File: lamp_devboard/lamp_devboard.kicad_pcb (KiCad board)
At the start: 2 copper layers, 127 parts, among them J101 Conn_02x02_Counter_Clockwise, J102 Conn_02x02_Counter_Clockwise, J103 Conn_02x02_Counter_Clockwise, J104 Conn_02x02_Counter_Clockwise, J105 Conn_02x02_Counter_Clockwise, J106 Conn_02x02_Counter_Clockwise, J201 Screw_Terminal_01x02, J202 USB_C_Receptacle_USB2.0, J203 Conn_01x03, J901 Conn_02x05_Odd_Even, J902 Conn_01x03, J903 Conn_01x06, J904 Conn_01x06, J905 Conn_01x06, J906 Conn_01x05, SW1001 SW_Push, SW1002 SW_Push, SW1003 SW_Push, U201 TPS212x, U202 BQ24200, U203 FUSB302B01MPX, U204 TLV71318PDBV, U205 TLV71318PDBV, U301 MAX9938, U401 TPS63060, U501 MAX9938, U601 TPS63060, U701 MAX9938, U901 STM32L476RG, Y901 Crystal_GND2, Y902 Crystal_GND2

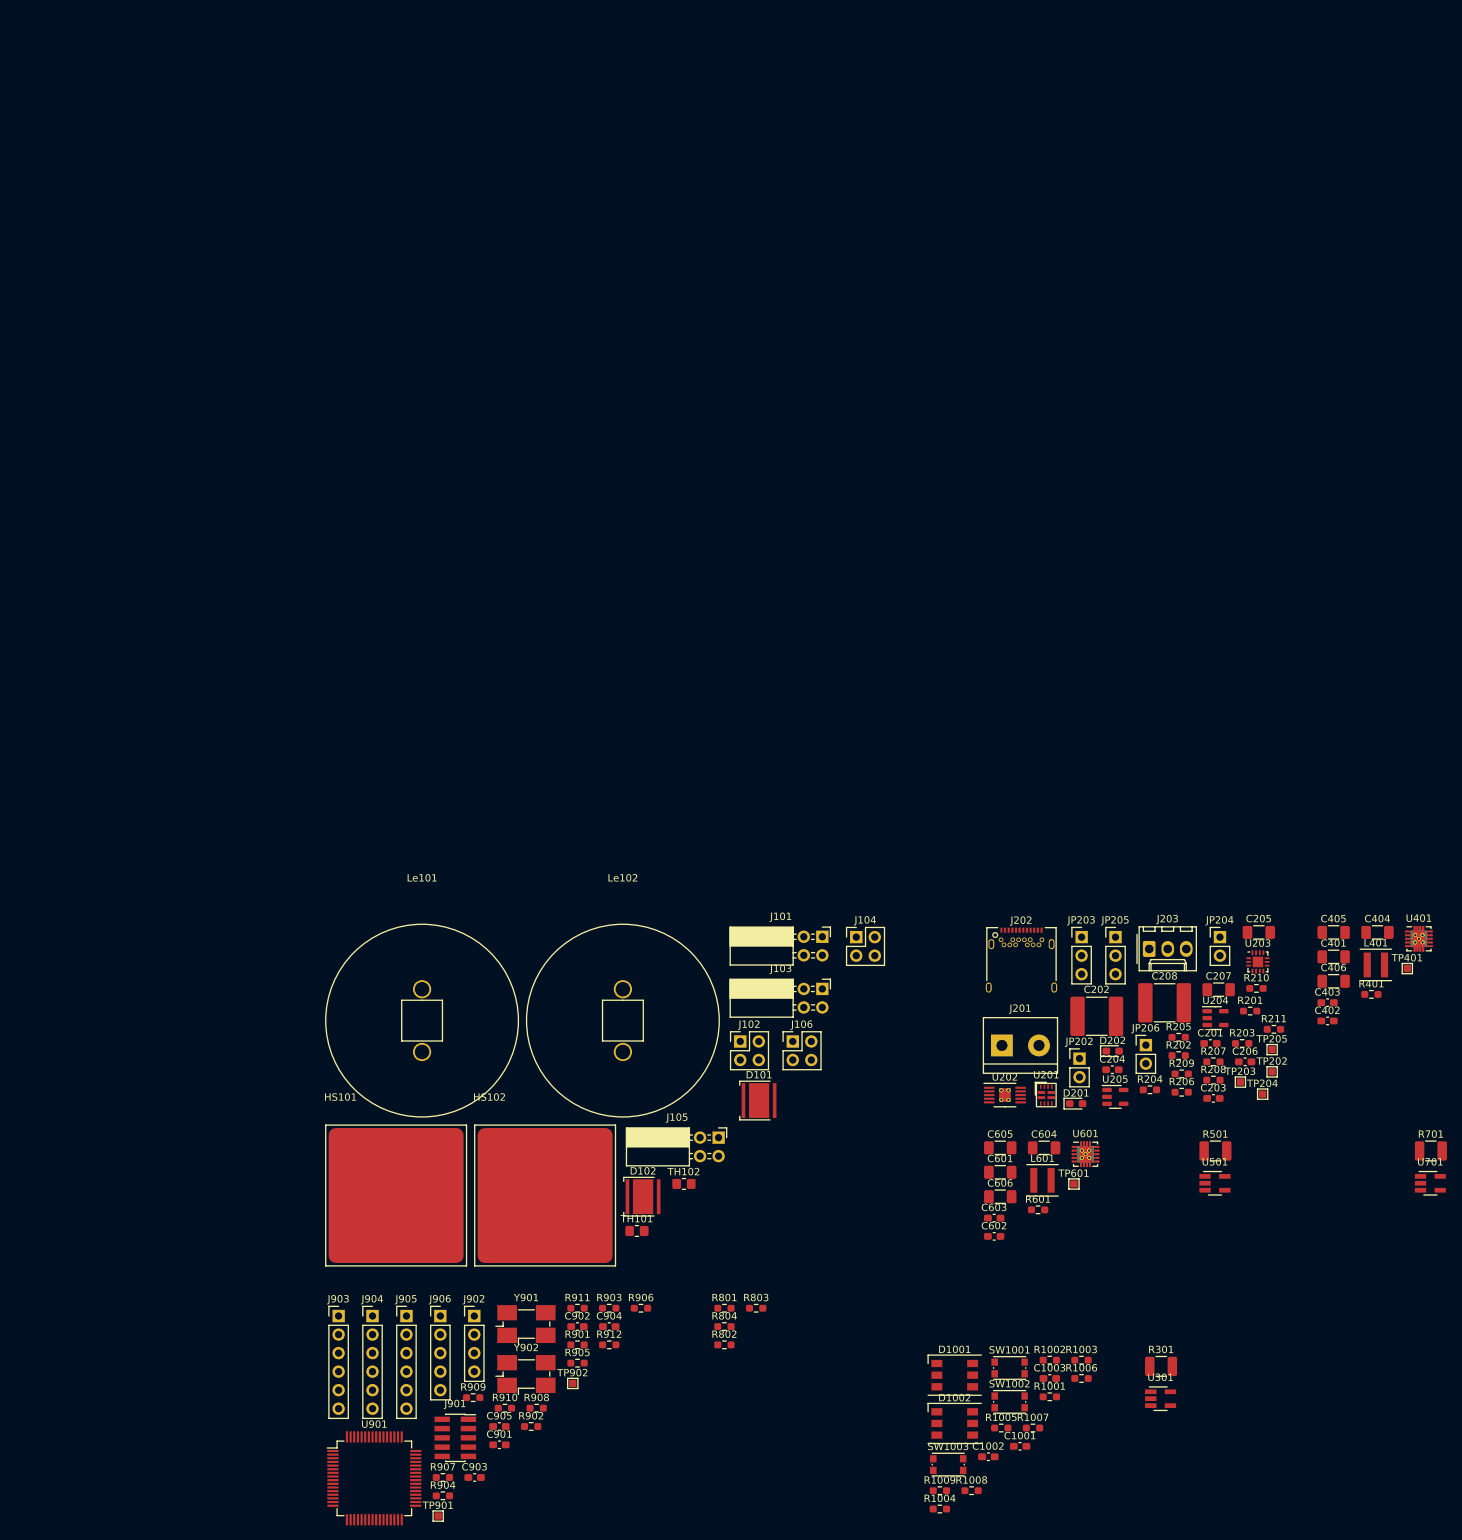
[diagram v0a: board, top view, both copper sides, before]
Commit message: place components
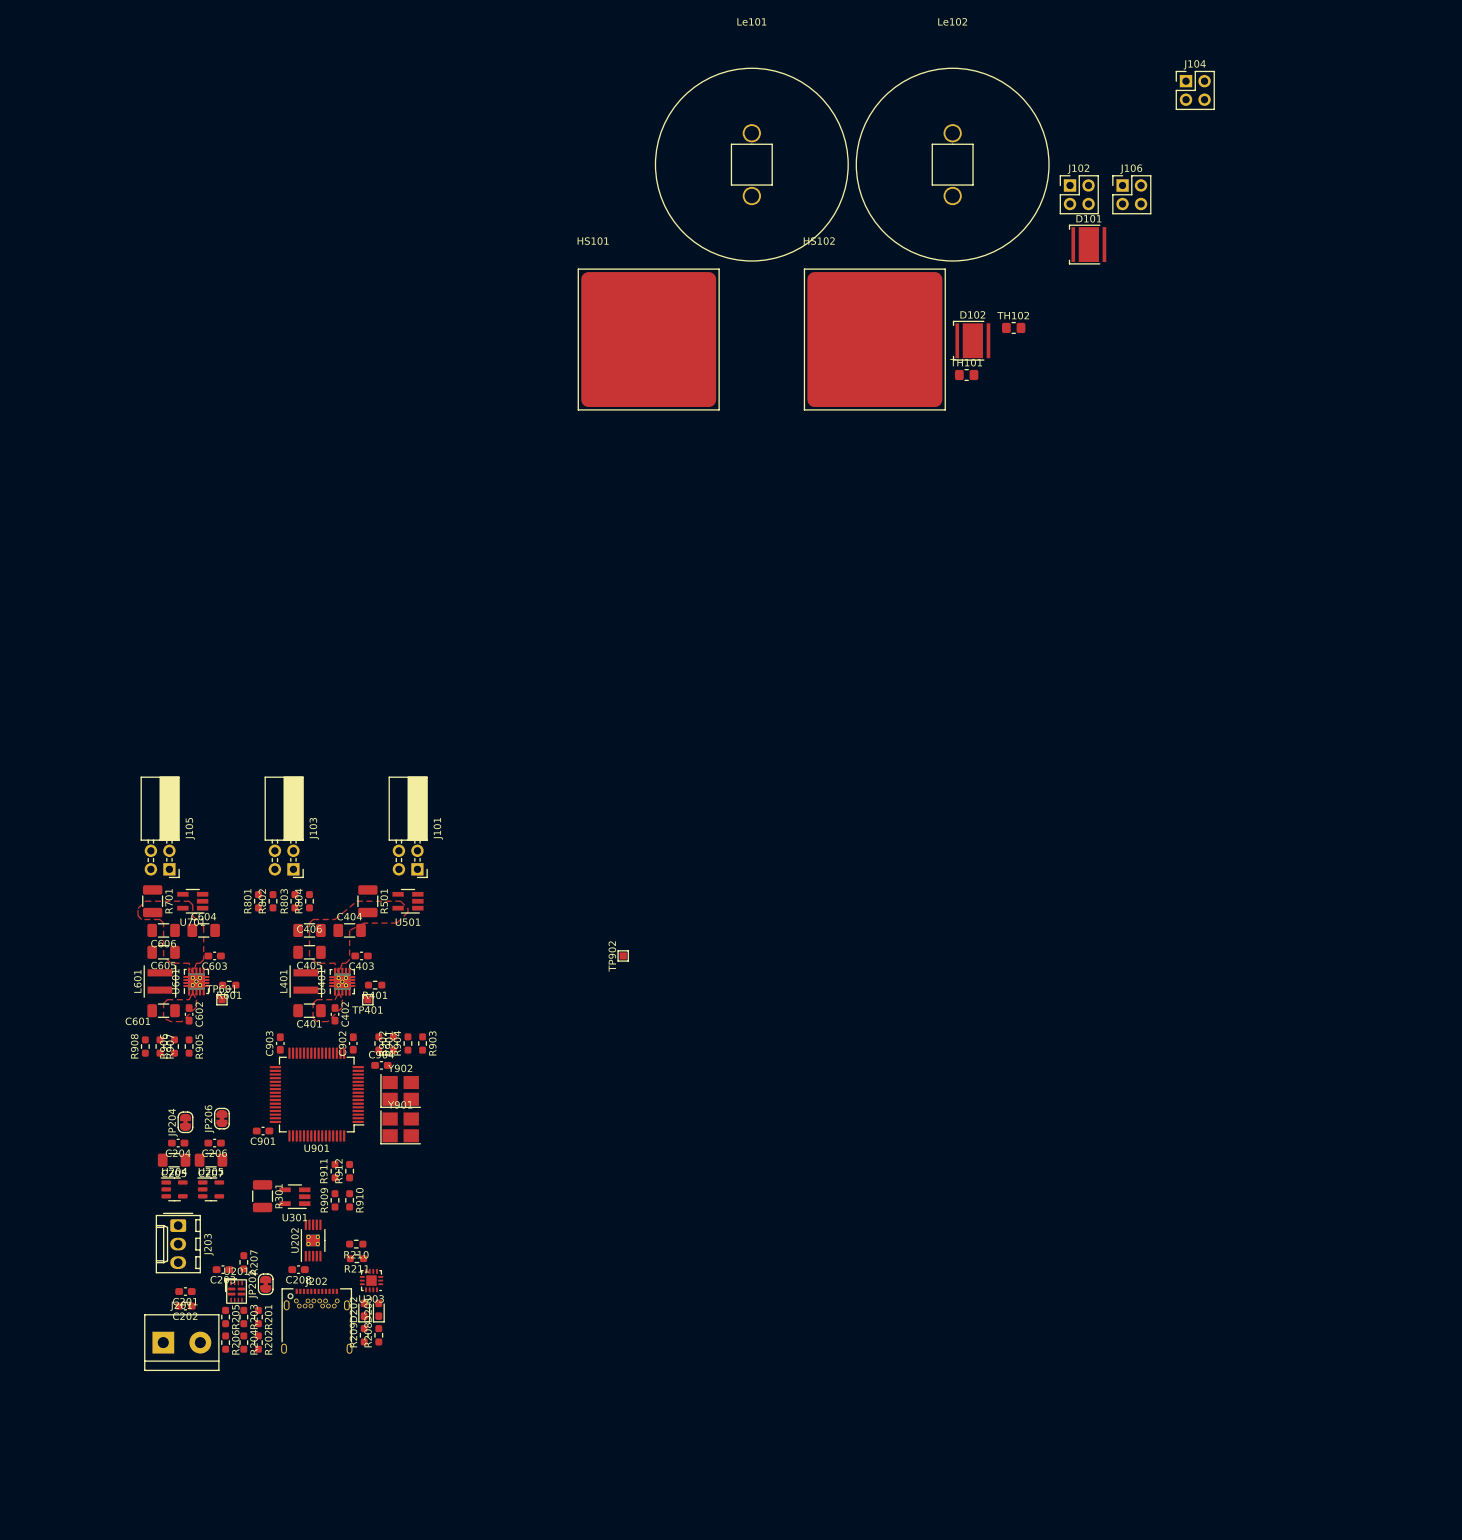
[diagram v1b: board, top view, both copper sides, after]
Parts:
- removed C1001, C1002, C1003, C905: C, Capacitor_SMD:C_0603_1608Metric_Pad1.08x0.95mm_HandSolder
- removed D1001, D1002: LED_RGB, LED_SMD:LED_WS2812_PLCC6_5.0x5.0mm_P1.6mm
- removed J901: Conn_02x05_Odd_Even, Connector_PinSocket_1.27mm:PinSocket_2x05_P1.27mm_Vertical_SMD
- removed J902: Conn_01x03, Connector_PinHeader_2.54mm:PinHeader_1x04_P2.54mm_Vertical
- removed J903, J904, J905: Conn_01x06, Connector_PinHeader_2.54mm:PinHeader_1x06_P2.54mm_Vertical
- removed J906: Conn_01x05, Connector_PinHeader_2.54mm:PinHeader_1x05_P2.54mm_Vertical
- removed JP203, JP205: Jumper_3_Open, Connector_PinHeader_2.54mm:PinHeader_1x03_P2.54mm_Vertical
- removed R1001, R1002, R1003, R1004, R1005, R1006, R1007, R1008, R1009: R, Resistor_SMD:R_0603_1608Metric_Pad0.98x0.95mm_HandSolder
- removed SW1001, SW1002, SW1003: SW_Push, Button_Switch_SMD:SW_Push_1P1T_NO_CK_KMR2
- removed TP202, TP203, TP204, TP205, TP901: TestPoint, TestPoint:TestPoint_Pad_1.0x1.0mm
- C202, C208: footprint Capacitor_SMD:C_2220_5650Metric_Pad1.97x5.40mm_HandSolder -> Capacitor_SMD:C_0603_1608Metric_Pad1.08x0.95mm_HandSolder
- JP202, JP204, JP206: footprint Connector_PinHeader_2.54mm:PinHeader_1x02_P2.54mm_Vertical -> Jumper:SolderJumper-2_P1.3mm_Bridged_RoundedPad1.0x1.5mm
- Y901, Y902: footprint Crystal:Crystal_SMD_0603-4Pin_6.0x3.5mm_HandSoldering -> Crystal:Crystal_SMD_3225-4Pin_3.2x2.5mm_HandSoldering
- moved R701 178.5 mm to (42.0, 42.5), turned to -90 degrees
- moved U701 174.0 mm to (47.5, 42.5), turned to 180 degrees
- moved C205 151.9 mm to (44.9, 78.0), turned to 180 degrees
- moved U401 147.7 mm to (68.0, 53.5), turned to 90 degrees
- moved L401 146.7 mm to (63.0, 53.5), turned to 90 degrees
- moved U204 144.6 mm to (45.0, 82.0)
- moved C201 144.6 mm to (46.5, 96.0), turned to 180 degrees
- moved JP204 144.1 mm to (46.5, 72.8), turned to 90 degrees
- moved TP401 142.6 mm to (71.5, 56.0), turned to 180 degrees
- moved R201 142.3 mm to (56.5, 99.5), turned to -90 degrees
- moved R203 141.9 mm to (54.5, 99.5), turned to -90 degrees
- moved C206 141.7 mm to (50.5, 75.7), turned to 180 degrees
- moved C404 140.9 mm to (69.0, 46.5)
- moved C401 140.6 mm to (63.5, 57.5), turned to 180 degrees
- moved C406 140.6 mm to (63.5, 46.5), turned to 180 degrees
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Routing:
- added copper zone on F.Cu, net /current_probe_1/IV_Iin
- added copper zone on F.Cu, net /current_probe_2/IV_Iin
- added copper zone on F.Cu, net /current_probe_in/IV_Iout

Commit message: add some power polygones to the pcb
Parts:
- moved J203 20.1 mm to (60.9, 99.9)
- moved JP202 7.82 mm to (57.0, 87.2)
- moved U202 6.05 mm to (61.7, 94.6), turned to -90 degrees
- moved R210 5.60 mm to (75.5, 89.5)
- moved D201 5.60 mm to (78.6, 98.5)
- moved D202 5.60 mm to (76.6, 98.5)
- moved R208 5.60 mm to (78.6, 102.0)
- moved R209 5.60 mm to (76.6, 102.0)
- moved R211 5.60 mm to (75.6, 91.5)
- moved U203 5.60 mm to (77.6, 94.5)
- moved J202 5.40 mm to (69.9, 101.0)
- moved C208 5.00 mm to (67.0, 93.0)
- moved JP206 2.12 mm to (49.4, 72.6)
- moved JP204 2.10 mm to (44.4, 72.8)
- moved C204 2.00 mm to (43.5, 75.7)
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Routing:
- net /current_probe_in/IV_Iin: track 0.00 -> 7.61 mm
- net Net-(C201-Pad1): track 0.00 -> 5.71 mm
- net /current_probe_in/IV_Out: track 0.00 -> 4.83 mm
- net Net-(J203-Pad1): track 0.00 -> 2.68 mm
- net /uC/Vout2: track 0.00 -> 2.00 mm
- net /uC/Vout1: track 0.00 -> 2.00 mm
- net /uC/Vin: track 0.00 -> 2.00 mm
- net /uC/Iout2: track 0.00 -> 2.00 mm
- net /uC/Iout1: track 0.00 -> 2.00 mm
- net /uC/Iin: track 0.00 -> 2.00 mm
- net Net-(D202-Pad1): track 0.00 -> 1.71 mm
- net Net-(D201-Pad1): track 0.00 -> 1.71 mm
- net Net-(R205-Pad2): track 0.00 -> 1.68 mm
- net Net-(R203-Pad2): track 0.00 -> 1.68 mm
- net Net-(R201-Pad2): track 0.00 -> 1.68 mm
- added copper zone on F.Cu, net (none)
- added copper zone on F.Cu, net /current_probe_1/IV_Iout
- added copper zone on F.Cu, net /current_probe_2/IV_Iout
- added copper zone on F.Cu, net /current_probe_in/IV_Iin
- added copper zone on F.Cu, net Net-(J203-Pad2)
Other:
- copper layers 2 -> 4

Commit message: add net classes, working on pcb layout
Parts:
- moved R207 5.61 mm to (53.5, 86.8)
- moved J202 5.61 mm to (69.6, 95.4)
- moved C201 5.61 mm to (46.2, 90.4)
- moved C202 5.61 mm to (46.2, 92.4)
- moved C203 5.61 mm to (49.8, 87.9)
- moved C208 5.61 mm to (66.7, 87.4)
- moved D201 5.61 mm to (78.3, 92.9)
- moved D202 5.61 mm to (76.3, 92.9)
- moved J201 5.61 mm to (43.2, 97.4)
- moved J203 5.61 mm to (60.6, 94.3)
- moved R201 5.61 mm to (56.2, 93.9)
- moved R202 5.61 mm to (56.2, 97.4)
- moved R203 5.61 mm to (54.2, 93.9)
- moved R204 5.61 mm to (54.2, 97.4)
- moved R205 5.61 mm to (51.7, 93.9)
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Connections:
- net Net-(C201-Pad1) renamed /power_in/TerminalPIn
- net Net-(C204-Pad1) renamed /power_in/V1_8_
- net Net-(C206-Pad1) renamed /power_in/V1_8A_
- net Net-(C208-Pad1) renamed /power_in/UsbPIn
- net Net-(J203-Pad1) renamed /power_in/BatP
- net Net-(JP202-Pad1) renamed /power_in/Pout_
- net Net-(L401-Pad1) renamed /dcdc1/L1
- net Net-(L401-Pad2) renamed /dcdc1/L2
- net Net-(L601-Pad1) renamed /dcdc2/L1
- net Net-(L601-Pad2) renamed /dcdc2/L2
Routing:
- net /current_probe_1/IV_Out: track 0.00 -> 28.6 mm
- net /1V8_D: track 0.00 -> 26.4 mm, vias 0 -> 10
- net /1V8_A: track 0.00 -> 19.8 mm, vias 0 -> 6
- net /current_probe_2/IV_Iin: track 0.00 -> 19.3 mm
- net /current_probe_1/IV_Iin: track 0.00 -> 19.0 mm
- net /power_in/TerminalPIn: track 5.71 -> 0.00 mm
- net /TC/TC_1+: track 0.00 -> 5.57 mm
- net /TC/TC_2+: track 0.00 -> 5.55 mm
- net Net-(D202-Pad1): track 1.71 -> 6.81 mm
- net Net-(D201-Pad1): track 1.71 -> 6.81 mm
- net Net-(R201-Pad2): track 1.68 -> 6.16 mm
- net /power_in/I2C.SCL: track 0.00 -> 4.12 mm
- net Net-(R205-Pad2): track 1.68 -> 5.46 mm
- net Net-(R203-Pad2): track 1.68 -> 5.25 mm
- net Net-(C203-Pad1): track 0.00 -> 2.99 mm
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- added copper zone on In2.Cu, net /1V8_A
- added copper zone on In2.Cu, net /1V8_D
- added copper zone on F.Cu, net /dcdc1/L1
- added copper zone on F.Cu, net /dcdc1/L2
- added copper zone on F.Cu, net /dcdc2/L1
- added copper zone on F.Cu, net /dcdc2/L2
- added copper zone on F.Cu, net /power_in/BatP
- added copper zone on F.Cu, net /power_in/V1_8_
- removed copper zone on F.Cu, net (none)
- removed copper zone on F.Cu, net Net-(J203-Pad2)

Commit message: some changes
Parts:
- removed TP902: TestPoint, TestPoint:TestPoint_Pad_1.0x1.0mm
- added C1001: C, Capacitor_SMD:C_0603_1608Metric_Pad1.08x0.95mm_HandSolder, B.Cu at (64.9, 58.8)
- added D1001: LED_RGB, LED_SMD:LED_WS2812_PLCC6_5.0x5.0mm_P1.6mm, B.Cu at (60.0, 68.8)
- added D203: SM6T12A, Diode_SMD:D_SMB, F.Cu at (42.4, 89.1)
- added F201: Fuse, Fuse:Fuse_1206_3216Metric_Pad1.42x1.75mm_HandSolder, F.Cu at (46.0, 90.3)
- added J1001: AudioJack4, Connector_Audio:Jack_3.5mm_CUI_SJ-3524-SMT_Horizontal, B.Cu at (45.9, 96.2)
- added J901: Conn_02x05_Odd_Even, Connector_PinSocket_1.27mm:PinSocket_2x05_P1.27mm_Vertical_SMD, B.Cu at (56.6, 80.6)
- added J905: Conn_01x06, Connector_PinHeader_2.54mm:PinHeader_1x06_P2.54mm_Vertical, B.Cu at (83.4, 75.5)
- added R1001: R, Resistor_SMD:R_0603_1608Metric_Pad0.98x0.95mm_HandSolder, B.Cu at (57.8, 54.6)
- added R1002: R, Resistor_SMD:R_0603_1608Metric_Pad0.98x0.95mm_HandSolder, F.Cu at (103.8, 98.3)
- added R1003: R, Resistor_SMD:R_0603_1608Metric_Pad0.98x0.95mm_HandSolder, F.Cu at (116.0, 76.6)
- added R1004: R, Resistor_SMD:R_0603_1608Metric_Pad0.98x0.95mm_HandSolder, B.Cu at (54.1, 70.4)
- added R1005: R, Resistor_SMD:R_0603_1608Metric_Pad0.98x0.95mm_HandSolder, B.Cu at (54.1, 68.8)
- added R1006: R, Resistor_SMD:R_0603_1608Metric_Pad0.98x0.95mm_HandSolder, B.Cu at (54.1, 67.2)
- added SW1001: SW_Push, Button_Switch_SMD:SW_Push_1P1T_NO_CK_KMR2, B.Cu at (59.9, 59.1)
- added U207: USBLC6-4SC6, Package_TO_SOT_SMD:SOT-23-6, B.Cu at (69.6, 95.4)
- moved J104 165.3 mm to (24.9, -23.7)
- moved J106 155.1 mm to (24.9, -16.5)
- moved J102 139.4 mm to (32.1, -23.7)
- moved D101 134.7 mm to (39.5, -15.6)
- moved D102 122.9 mm to (33.0, -15.6)
- moved TH101 108.7 mm to (45.0, -24.6)
- moved Le102 89.8 mm to (63.9, -39.8)
- moved Le101 89.8 mm to (36.3, -39.8)
- moved TH102 61.7 mm to (100.4, -52.1)
- moved HS102 54.4 mm to (87.8, -23.0)
- moved HS101 23.9 mm to (87.8, -43.4)
- moved C202 6.50 mm to (47.8, 86.1), turned to 90 degrees
- moved C201 4.30 mm to (46.1, 86.1), turned to 90 degrees
- moved C203 2.28 mm to (51.8, 86.8), turned to 90 degrees
- moved C901 1.11 mm to (58.0, 74.7), turned to -90 degrees
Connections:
- net /io/IO_BUTTONS1 renamed /uC/UC_BUTTONS1
- net /io/IO_BUTTONS2 renamed /uC/UC_BUTTONS2
- J201 pad 2: /power_in/TerminalPIn -> /power_in/TerminalPIn_
- J202 pad A8: Net-(J202-PadA8) -> unconnected-(J202-PadA8)
- J202 pad B8: Net-(J202-PadB8) -> unconnected-(J202-PadB8)
- R201 pad 1: /power_in/TerminalPIn -> /power_in/BatP
- R203 pad 1: /power_in/TerminalPIn -> /power_in/BatP
- R205 pad 1: /power_in/BatP -> /power_in/TerminalPIn
- U201 pad 2: /power_in/BatP -> /power_in/TerminalPIn
- U201 pad 7: /power_in/TerminalPIn -> /power_in/BatP
- U203 pad 12: Net-(TP205-Pad1) -> unconnected-(U203-Pad12)
- U203 pad 13: Net-(TP205-Pad1) -> unconnected-(U203-Pad12)
- U203 pad 5: Net-(TP202-Pad1) -> unconnected-(U203-Pad5)
- U204 pad 3: Net-(JP203-Pad2) -> /power_in/Pout_
- U205 pad 3: Net-(JP205-Pad2) -> /power_in/Pout_
- U901 pad 33: Net-(J906-Pad1) -> unconnected-(U901-Pad33)
- U901 pad 34: Net-(J906-Pad2) -> unconnected-(U901-Pad34)
- U901 pad 35: /io/IO_LEDRGBS6 -> unconnected-(U901-Pad35)
- U901 pad 36: /io/IO_LEDRGBS5 -> unconnected-(U901-Pad36)
- U901 pad 37: /io/IO_LEDRGBS4 -> unconnected-(U901-Pad37)
- U901 pad 43: /io/IO_BUTTONS3 -> unconnected-(U901-Pad43)
- U901 pad 51: Net-(J906-Pad3) -> unconnected-(U901-Pad51)
- U901 pad 52: Net-(J906-Pad4) -> unconnected-(U901-Pad52)
- U901 pad 53: Net-(J906-Pad5) -> unconnected-(U901-Pad53)
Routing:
- net GND: track 0.00 -> 111.9 mm, vias 0 -> 63
- net /1V8_D: track 26.4 -> 83.9 mm, vias 10 -> 13
- net /power_in/USB_DATA.D-: track 0.00 -> 54.2 mm
- net /power_in/USB_DATA.D+: track 0.00 -> 47.4 mm, vias 0 -> 2
- net /dcdc2/DCDC_F: track 0.00 -> 35.7 mm, vias 0 -> 2
- net /TC/TC_1+: track 5.57 -> 39.0 mm, vias 0 -> 2
- net Net-(J202-PadA5): track 0.00 -> 29.5 mm, vias 0 -> 2
- net /power_in/BAT_STATE: track 0.00 -> 28.0 mm, vias 0 -> 2
- net /uC/Iout2: track 2.00 -> 29.2 mm, vias 0 -> 2
- net /power_in/SWITCH_STATE: track 0.00 -> 25.8 mm, vias 0 -> 2
- net /current_probe_2/IV_Out: track 0.00 -> 25.0 mm, vias 0 -> 2
- net unconnected-(U901-Pad51): track 0.00 -> 24.6 mm
- net /dcdc2/DCDC_PG: track 0.00 -> 24.6 mm, vias 0 -> 2
- net /dcdc2/DCDC_EN: track 0.00 -> 23.9 mm, vias 0 -> 2
- net /io/IO_BUTTONS1: track 0.00 -> 23.8 mm, vias 0 -> 2
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- added copper zone on F.Cu, net /power_in/Pout_
- added copper zone on F.Cu, net /power_in/TerminalPIn
- added copper zone on F.Cu, net /power_in/TerminalPIn_
- added copper zone on F.Cu, net /power_in/UsbPIn
- added copper zone on In2.Cu, net /power_in/UsbPIn
- added copper zone on F.Cu, net /power_in/V1_8A_
- added copper zone on F.Cu, net GND
- added copper zone on In1.Cu, net GND
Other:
- board outline added: 40 x 66.8 mm
